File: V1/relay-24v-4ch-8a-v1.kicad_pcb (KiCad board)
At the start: 2 copper layers, 53 x 67.8 mm, 25 parts, among them J1 250-202, J2 250-204, J3 DB142V-5.08-4P, J4 DB142V-5.08-4P, K1 G5Q-1A4-DC24V, K2 G5Q-1A4-DC24V, K3 G5Q-1A4-DC24V, K4 G5Q-1A4-DC24V

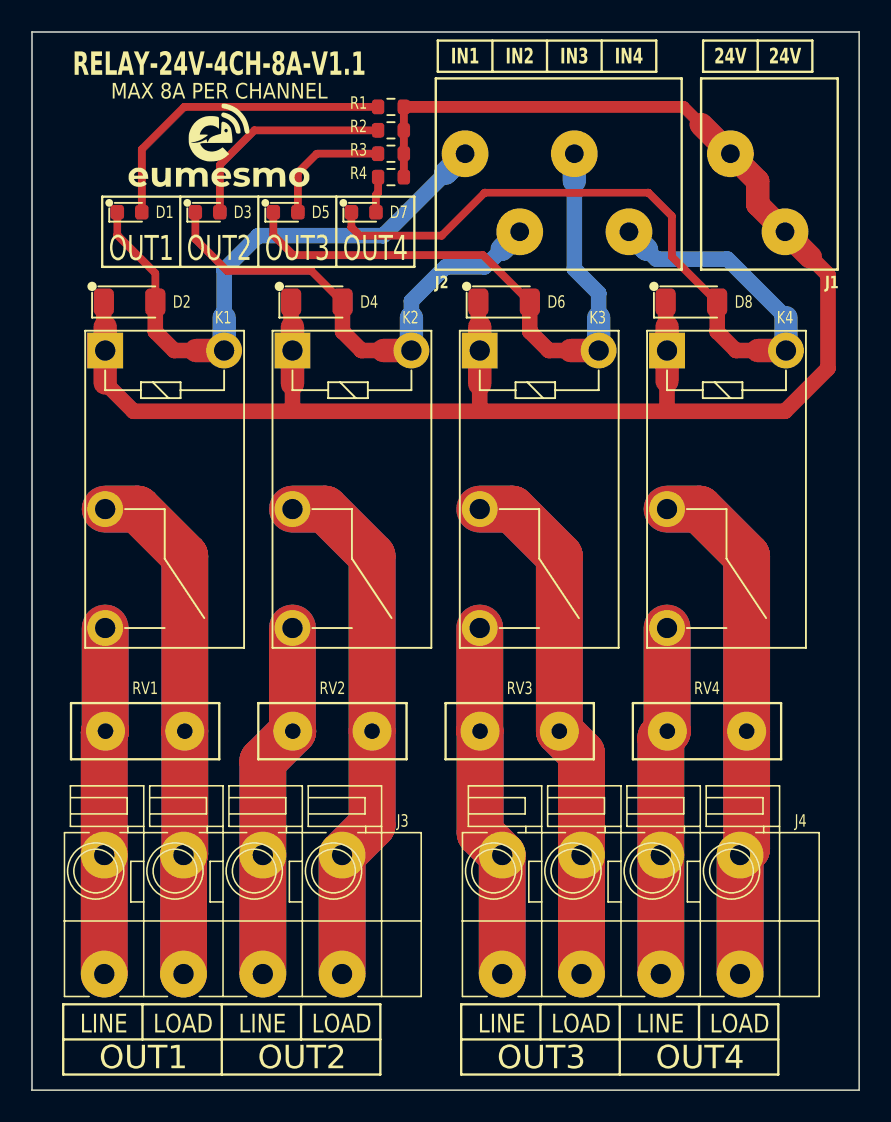
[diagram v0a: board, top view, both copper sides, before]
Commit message: Replaced input terminal blocks for 3.5mm pitch.
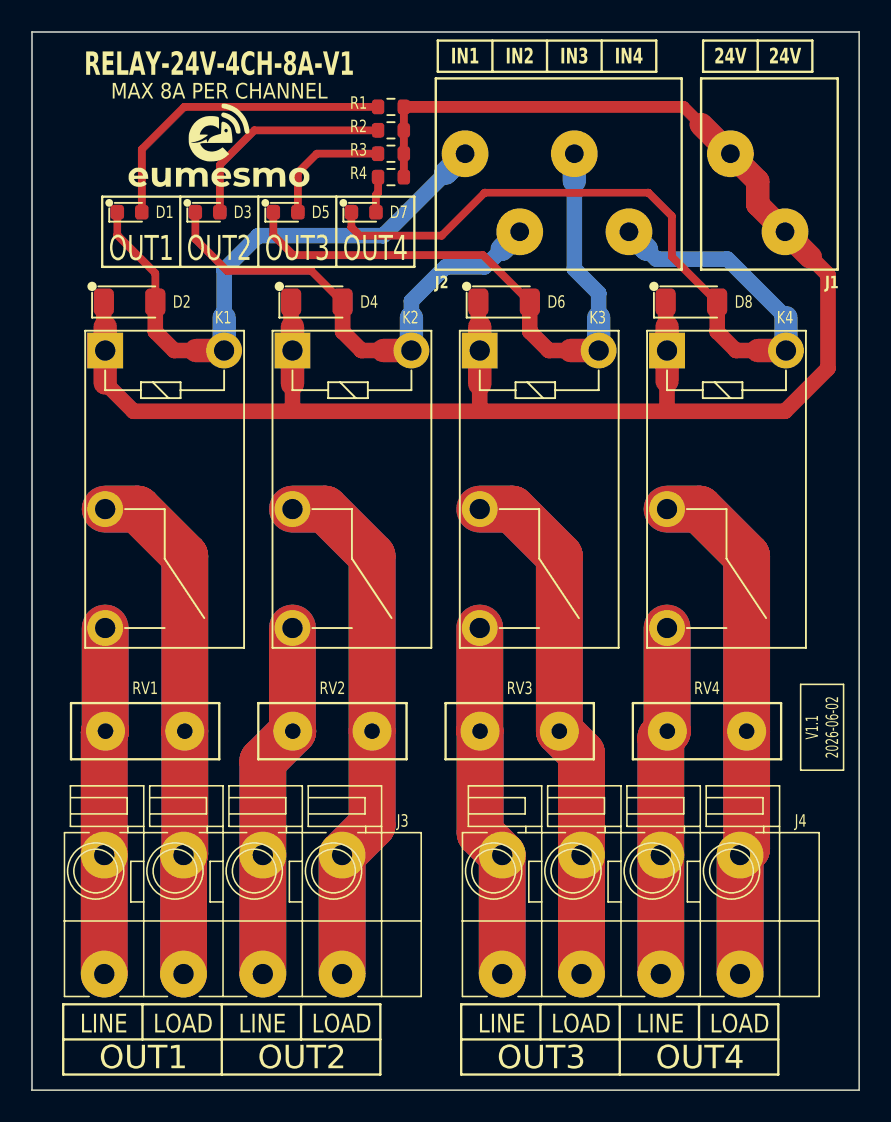
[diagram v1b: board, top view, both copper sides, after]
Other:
- board text added: "RELAY-24V-4CH-8A-V1"
- board text added: "V1.1 2026-06-02"
- board text removed: "RELAY-24V-4CH-8A-V1.1"
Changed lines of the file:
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@@
 	(title_block
 		(title "4x 24V 8A Relay Module")
-		(date "2026-06-01")
+		(date "2026-06-02")
 		(rev "V1.1")
 	)
@@
 			)
 		)
-		(property "Mfr" "DORABO"
+		(property "Mfr" "Wago"
 			(at 0 0 180)
 			(unlocked yes)
@@
 			)
 		)
-		(property "Mfr" "DORABO"
+		(property "Mfr" "Wago"
 			(at 0 0 180)
 			(unlocked yes)
@@
 	)
 	(gr_rect
+		(start 174.25 104)
+		(end 177 109.5)
+		(stroke
+			(width 0.1)
+			(type solid)
+		)
+		(fill no)
+		(layer "F.SilkS")
+	)
+	(gr_rect
 		(start 125 62.2)
 		(end 178 130)
@@
 		(layer "Edge.Cuts")
 	)
+	(gr_text "V1.1\n2026-06-02"
+		(at 176.75 106.75 90)
+		(layer "F.SilkS")
+		(effects
+			(font
+				(size 0.8 0.5)
+				(thickness 0.1)
+			)
+			(justify bottom)
+		)
+	)
 	(gr_text "IN1"
 		(at 152.75 63.75 0)
@@
 		)
 	)
-	(gr_text "RELAY-24V-4CH-8A-V1.1"
+	(gr_text "RELAY-24V-4CH-8A-V1"
 		(at 137 64.25 0)
 		(layer "F.SilkS")
